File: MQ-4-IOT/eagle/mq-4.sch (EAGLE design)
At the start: 1 part

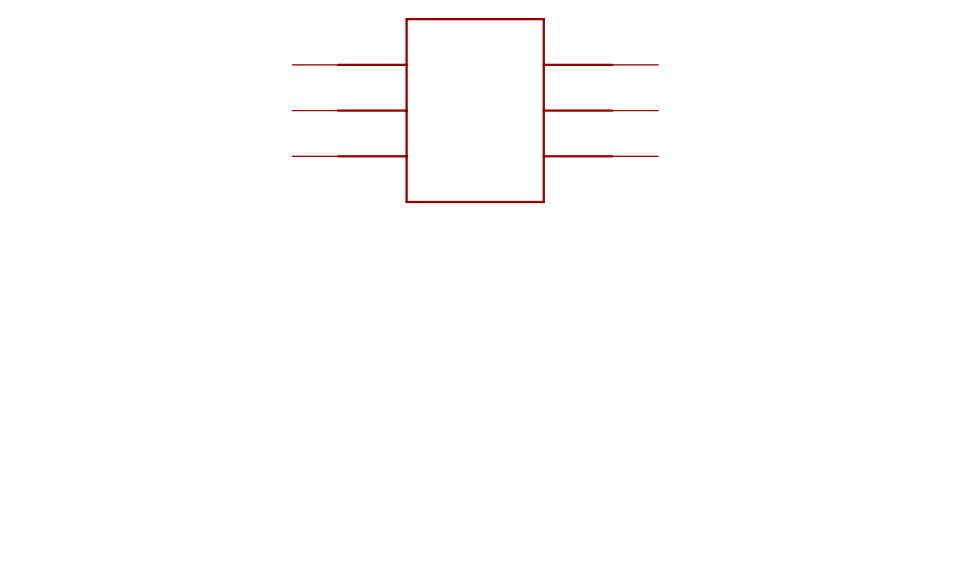
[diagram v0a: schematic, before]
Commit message: MQ-4 breakout added.
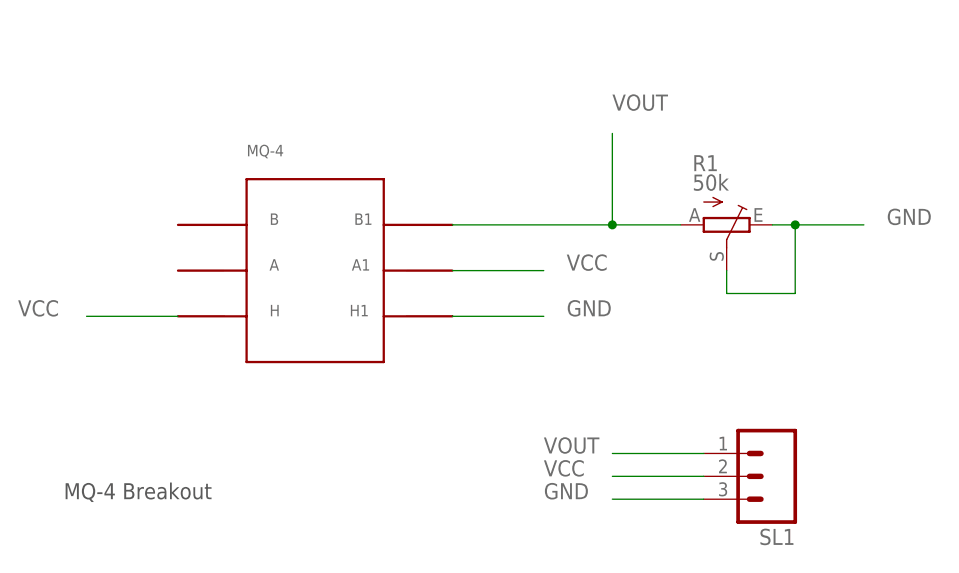
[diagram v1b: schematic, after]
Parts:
- added R1: 50k, pot:TRIM_EU-B64Y
- added SL1: (no value), con-amp-quick:M03
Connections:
- new net GND: R1.E, R1.S, SL1.3, U$1.H1
- new net VCC: SL1.2, U$1.A1, U$1.H
- new net VOUT: R1.A, SL1.1, U$1.B1
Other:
- note added: "MQ-4 Breakout"
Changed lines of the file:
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@@
 </variantdefs>
 <classes>
-<class number="0" name="default" width="0" drill="0">
+<class number="0" name="default" width="1.27" drill="0.6096">
+<clearance class="0" value="0.508"/>
+</class>
+<class number="1" name="gnd" width="0.9144" drill="0.254">
 </class>
 </classes>
 <parts>
 <part name="U$1" library="mq-x" deviceset="MQ-4" device=""/>
+<part name="R1" library="pot" deviceset="TRIM_EU-" device="B64Y" value="50k"/>
+<part name="SL1" library="con-amp-quick" deviceset="M03" device=""/>
 </parts>
 <sheets>
 <sheet>
 <plain>
+<text x="25.4" y="20.32" size="1.778" layer="97">MQ-4 Breakout</text>
 </plain>
 <instances>
-<instance part="U$1" gate="G$1" x="71.12" y="63.5"/>
+<instance part="U$1" gate="G$1" x="53.34" y="45.72"/>
+<instance part="R1" gate="1" x="99.06" y="50.8" rot="R270"/>
+<instance part="SL1" gate="G$1" x="104.14" y="22.86" rot="R180"/>
 </instances>
 <busses>
 </busses>
 <nets>
+<net name="VCC" class="0">
+<segment>
+<pinref part="U$1" gate="G$1" pin="H"/>
+<wire x1="38.1" y1="40.64" x2="27.94" y2="40.64" width="0.1524" layer="91"/>
+<label x="20.32" y="40.64" size="1.778" layer="95"/>
+</segment>
+<segment>
+<pinref part="U$1" gate="G$1" pin="A1"/>
+<wire x1="68.58" y1="45.72" x2="78.74" y2="45.72" width="0.1524" layer="91"/>
+<label x="81.28" y="45.72" size="1.778" layer="95"/>
+</segment>
+<segment>
+<pinref part="SL1" gate="G$1" pin="2"/>
+<wire x1="96.52" y1="22.86" x2="86.36" y2="22.86" width="0.1524" layer="91"/>
+<label x="78.74" y="22.86" size="1.778" layer="95"/>
+</segment>
+</net>
+<net name="GND" class="1">
+<segment>
+<pinref part="R1" gate="1" pin="E"/>
+<wire x1="104.14" y1="50.8" x2="106.68" y2="50.8" width="0.1524" layer="91"/>
+<label x="116.84" y="50.8" size="1.778" layer="95"/>
+<pinref part="R1" gate="1" pin="S"/>
+<wire x1="106.68" y1="50.8" x2="114.3" y2="50.8" width="0.1524" layer="91"/>
+<wire x1="99.06" y1="45.72" x2="99.06" y2="43.18" width="0.1524" layer="91"/>
+<wire x1="99.06" y1="43.18" x2="106.68" y2="43.18" width="0.1524" layer="91"/>
+<wire x1="106.68" y1="43.18" x2="106.68" y2="50.8" width="0.1524" layer="91"/>
+<junction x="106.68" y="50.8"/>
+</segment>
+<segment>
+<pinref part="U$1" gate="G$1" pin="H1"/>
+<wire x1="68.58" y1="40.64" x2="78.74" y2="40.64" width="0.1524" layer="91"/>
+<label x="81.28" y="40.64" size="1.778" layer="95"/>
+</segment>
+<segment>
+<pinref part="SL1" gate="G$1" pin="3"/>
+<wire x1="96.52" y1="20.32" x2="86.36" y2="20.32" width="0.1524" layer="91"/>
+<label x="78.74" y="20.32" size="1.778" layer="95"/>
+</segment>
+</net>
+<net name="VOUT" class="0">
+<segment>
+<pinref part="SL1" gate="G$1" pin="1"/>
+<wire x1="96.52" y1="25.4" x2="86.36" y2="25.4" width="0.1524" layer="91"/>
+<label x="78.74" y="25.4" size="1.778" layer="95"/>
+</segment>
+<segment>
+<pinref part="U$1" gate="G$1" pin="B1"/>
+<pinref part="R1" gate="1" pin="A"/>
+<wire x1="93.98" y1="50.8" x2="86.36" y2="50.8" width="0.1524" layer="91"/>
+<wire x1="86.36" y1="50.8" x2="68.58" y2="50.8" width="0.1524" layer="91"/>
+<wire x1="86.36" y1="50.8" x2="86.36" y2="60.96" width="0.1524" layer="91"/>
+<junction x="86.36" y="50.8"/>
+<label x="86.36" y="63.5" size="1.778" layer="95"/>
+</segment>
+</net>
 </nets>
 </sheet>
